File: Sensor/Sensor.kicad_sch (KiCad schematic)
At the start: 17 parts, among them J1 Signal, J2 Power, U1 LBR-127HLD, U2 LBR-127HLD, U3 LBR-127HLD, U4 LBR-127HLD, U5 LBR-127HLD

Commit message: センサー関係忘れてた
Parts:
- added D1, D2, D3, D4, D5: LED, LED_SMD:LED_0603_1608Metric, symbol Device:LED
- added U6: 74HC244, Package_SO:SSOP-20_4.4x6.5mm_P0.65mm, symbol 74xx:74HC244
- R1: value 200 -> 220; footprint Resistor_THT:R_Axial_DIN0207_L6.3mm_D2.5mm_P10.16mm_Horizontal -> Resistor_SMD:R_0603_1608Metric
- R10, R2, R3, R4, R5, R6, R7, R8, R9: footprint Resistor_THT:R_Axial_DIN0207_L6.3mm_D2.5mm_P10.16mm_Horizontal -> Resistor_SMD:R_0603_1608Metric
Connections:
- net GND: now also U1.3 (Emitter), U2.3 (Emitter), U3.3 (Emitter), U4.3 (Emitter), U5.3 (Emitter), D1.1 (K), D2.1 (K), D3.1 (K), D4.1 (K), D5.1 (K), U6.1 (1OE), U6.10 (GND), U6.19 (2OE); no longer U1.4 (Collector), U2.4 (Collector), U3.4 (Collector), U4.4 (Collector), U5.4 (Collector)
- net O1: now also U1.4 (Collector), U6.2 (1A0); no longer U1.3 (Emitter)
- net O2: now also U2.4 (Collector), U6.4 (1A1); no longer U2.3 (Emitter)
- net O3: now also U3.4 (Collector), U6.6 (1A2); no longer U3.3 (Emitter)
- net O4: now also U4.4 (Collector), U6.8 (1A3); no longer U4.3 (Emitter)
- net O5: now also U5.4 (Collector), U6.17 (2A0); no longer U5.3 (Emitter)
- net VCC: now also U6.20 (VCC)
- new net: D2.2 (A), U6.16 (1Y1)
- new net: D5.2 (A), U6.3 (2Y0)
- new net: D1.2 (A), U6.18 (1Y0)
- new net: D3.2 (A), U6.14 (1Y2)
- new net: D4.2 (A), U6.12 (1Y3)
- no-connect marks 0 -> 6
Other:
- moved on the sheet: R2, R3, R5, R7, R9

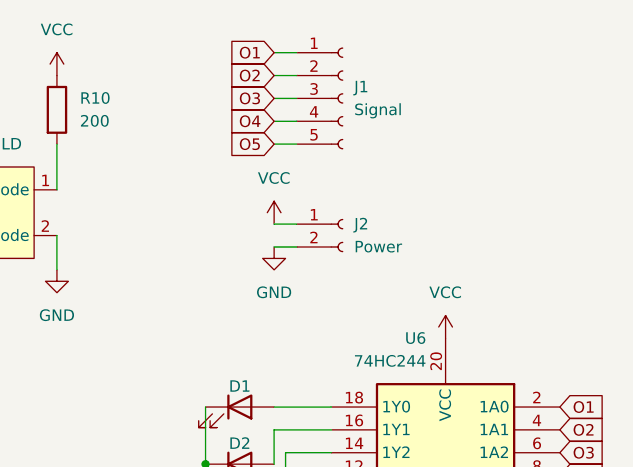
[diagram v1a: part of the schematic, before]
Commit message: 出力を追加
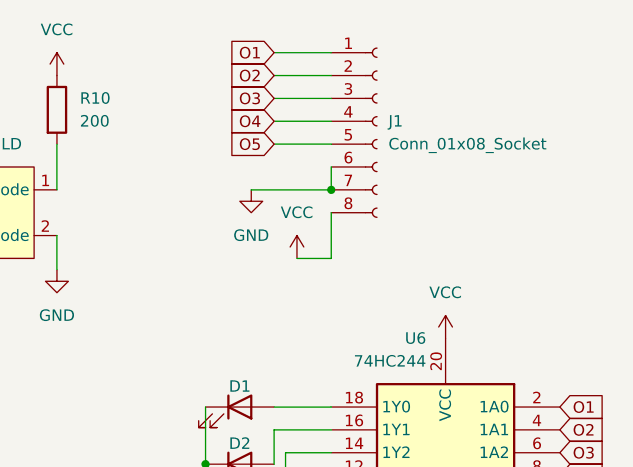
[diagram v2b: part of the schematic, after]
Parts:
- removed J1: Signal, Connector_PinSocket_2.54mm:PinSocket_1x05_P2.54mm_Vertical, symbol Connector:Conn_01x05_Socket
- removed J2: Power, Connector_PinSocket_2.54mm:PinSocket_1x02_P2.54mm_Vertical, symbol Connector:Conn_01x02_Socket
- added J1: Conn_01x08_Socket, Connector_PinSocket_2.54mm:PinSocket_1x08_P2.54mm_Vertical, symbol Connector:Conn_01x08_Socket
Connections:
- net GND: now also J1.6 (Pin_6), J1.7 (Pin_7)
- net O1: now also J1.1 (Pin_1)
- net O2: now also J1.2 (Pin_2)
- net O3: now also J1.3 (Pin_3)
- net O4: now also J1.4 (Pin_4)
- net O5: now also J1.5 (Pin_5)
- net VCC: now also J1.8 (Pin_8)
